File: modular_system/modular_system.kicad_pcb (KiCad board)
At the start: 2 copper layers, 97.2 x 48.5 mm, 12 parts, among them J1 Screw_Terminal_01x02, J2 Conn_01x01_Male, J3 Conn_01x01_Male, J4 Conn_01x01_Male, J5 Conn_01x01_Male, J6 Conn_01x04_Female, J7 Conn_01x04_Female, U1 BluePill_STM32F103C

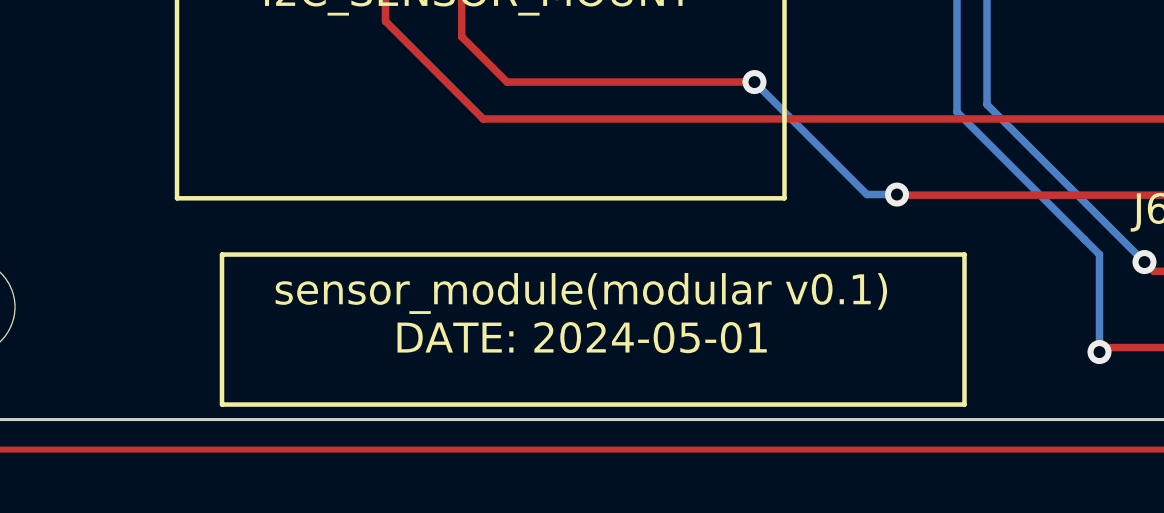
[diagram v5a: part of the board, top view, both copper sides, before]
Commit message: updated silkscreen
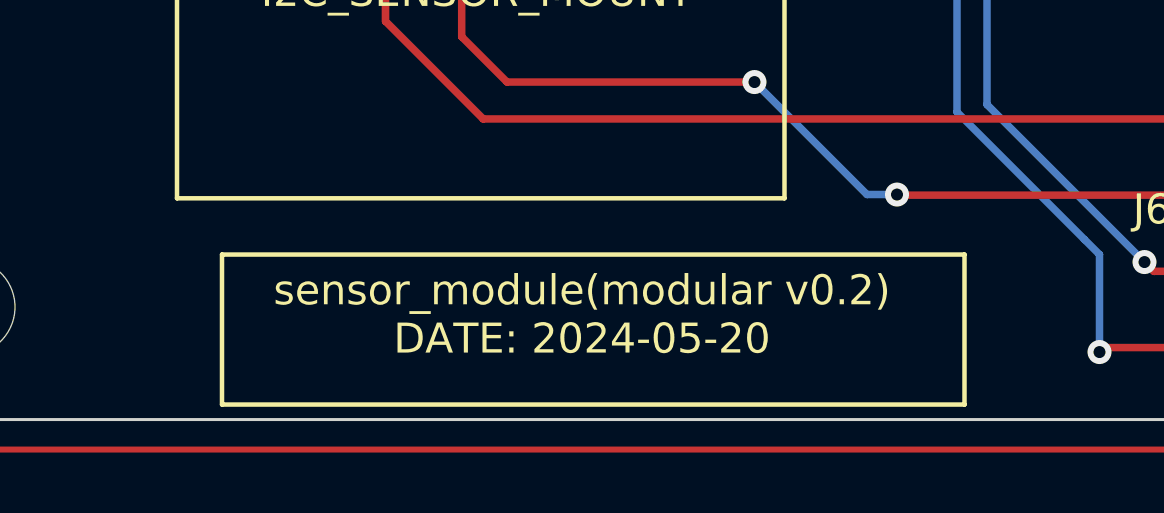
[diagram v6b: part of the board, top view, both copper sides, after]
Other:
- board text added: "sensor_module(modular v0.2) DATE: 2024-05-20"
- board text removed: "sensor_module(modular v0.1) DATE: 2024-05-01"
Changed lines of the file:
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@@
     (effects (font (size 1 1) (thickness 0.15)))
   )
-  (gr_text "sensor_module(modular v0.1)\nDATE: 2024-05-01" (at 124.25 95.5) (layer "F.SilkS")
+  (gr_text "sensor_module(modular v0.2)\nDATE: 2024-05-20" (at 124.25 95.5) (layer "F.SilkS")
     (effects (font (size 1 1) (thickness 0.15)))
   )
